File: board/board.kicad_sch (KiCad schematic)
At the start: 10 parts, among them U2 Adafruit_Feather_nRF52_Bluefr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

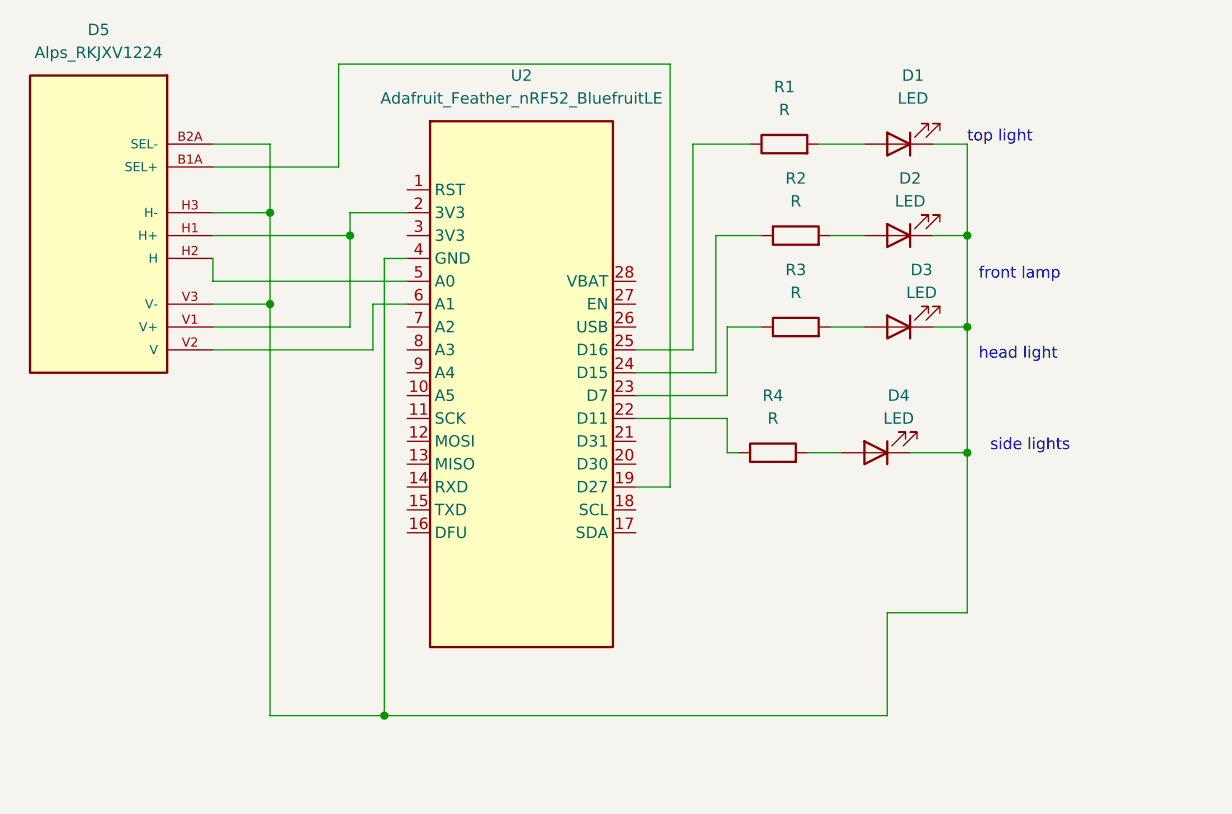
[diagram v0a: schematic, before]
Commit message: * board: Add usb pin and second side light led
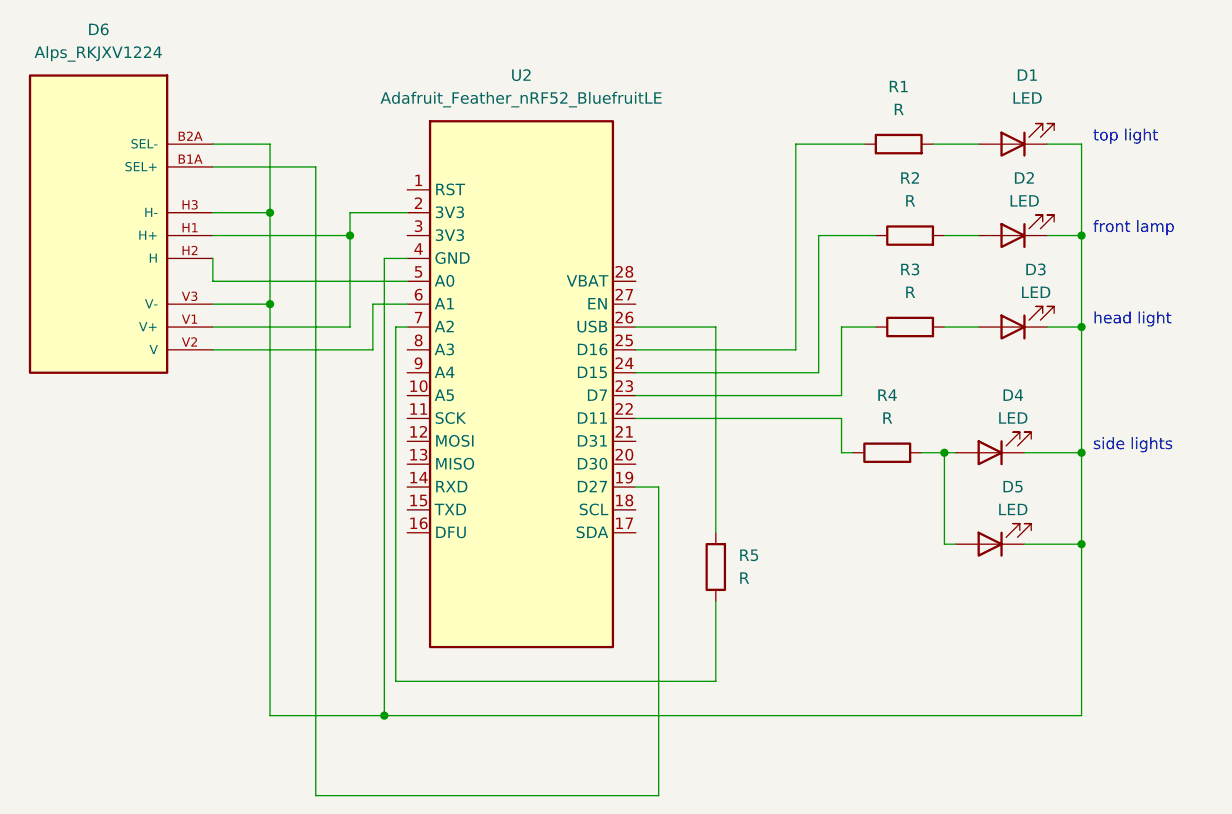
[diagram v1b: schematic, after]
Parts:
- added D5: LED, LED_THT:LED_D5.0mm_Clear, symbol Device:LED
- added R5: R, Resistor_THT:R_Axial_DIN0207_L6.3mm_D2.5mm_P10.16mm_Horizontal, symbol Device:R
- renumbered D5 to D6
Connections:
- net at U2.26 (USB): now also R5.2
- net at D1.1 (K), D2.1 (K), D3.1 (K)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: now also D5.1 (K)
- net at U2.7 (A2): now also R5.1
- net at D4.2 (A), R4.2: now also D5.2 (A)
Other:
- moved on the sheet: D1, D2, D3, D4, R1, R2, R3, R4
